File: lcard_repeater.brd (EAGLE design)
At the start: 100 x 80 mm, 90 parts, among them X1 236-741-5,08, X10 236-741-5,08, X11 236-741-5,08, X12 236-741-5,08, X13 236-741-5,08, X14 236-741-5,08, X15 236-741-5,08, X16 236-741-5,08, X17 236-741-5,08, X18 236-741-5,08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

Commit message: попытка развести плату
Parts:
- moved R1 11.6 mm to (39.4, 9.49)
- moved R10 11.6 mm to (35.6, 22.2)
- moved R11 11.6 mm to (31.8, 24.7)
- moved R13 11.6 mm to (39.4, 28.5)
- moved R14 11.6 mm to (35.6, 28.5)
- moved R15 11.6 mm to (31.8, 31.1)
- moved R17 11.6 mm to (39.4, 34.9)
- moved R18 11.6 mm to (35.6, 34.9)
- moved R19 11.6 mm to (31.8, 37.4)
- moved R2 11.6 mm to (35.6, 9.49)
- moved R21 11.6 mm to (39.4, 41.2)
- moved R22 11.6 mm to (35.6, 41.2)
- moved R23 11.6 mm to (31.8, 43.8)
- moved R25 11.6 mm to (39.4, 47.6), turned to 270 degrees
- moved R26 11.6 mm to (35.6, 47.6), turned to 270 degrees
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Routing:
- net GND: track 0.00 -> 98.8 mm, vias 0 -> 12
- net DAC1: track 0.00 -> 95.2 mm
- net DAC2: track 0.00 -> 58.2 mm
- net LY10: track 0.00 -> 50.3 mm, vias 0 -> 1
- net LY9: track 0.00 -> 47.1 mm, vias 0 -> 1
- net LY8: track 0.00 -> 43.2 mm, vias 0 -> 1
- net LY7: track 0.00 -> 40.0 mm, vias 0 -> 1
- net LX10: track 0.00 -> 35.9 mm
- net LY6: track 0.00 -> 35.6 mm, vias 0 -> 1
- net LX9: track 0.00 -> 32.2 mm
- net LY5: track 0.00 -> 30.6 mm, vias 0 -> 1
- net LY1: track 0.00 -> 30.3 mm, vias 0 -> 1
- net LY4: track 0.00 -> 29.1 mm, vias 0 -> 1
- net LX8: track 0.00 -> 28.7 mm
- net LY2: track 0.00 -> 26.8 mm, vias 0 -> 1
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
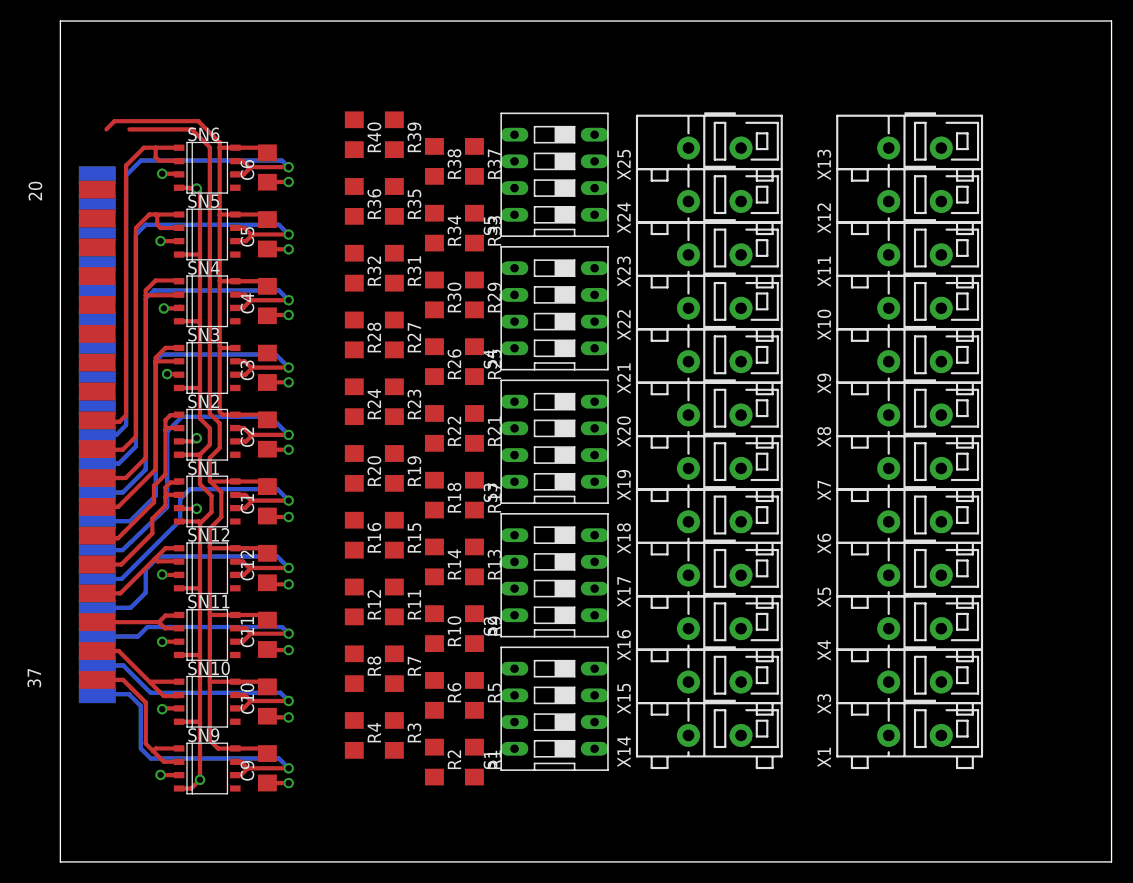
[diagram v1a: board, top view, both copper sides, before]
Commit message: почти развел плату, осталось немного. необходимо подсоединить конденсаторы по питанию
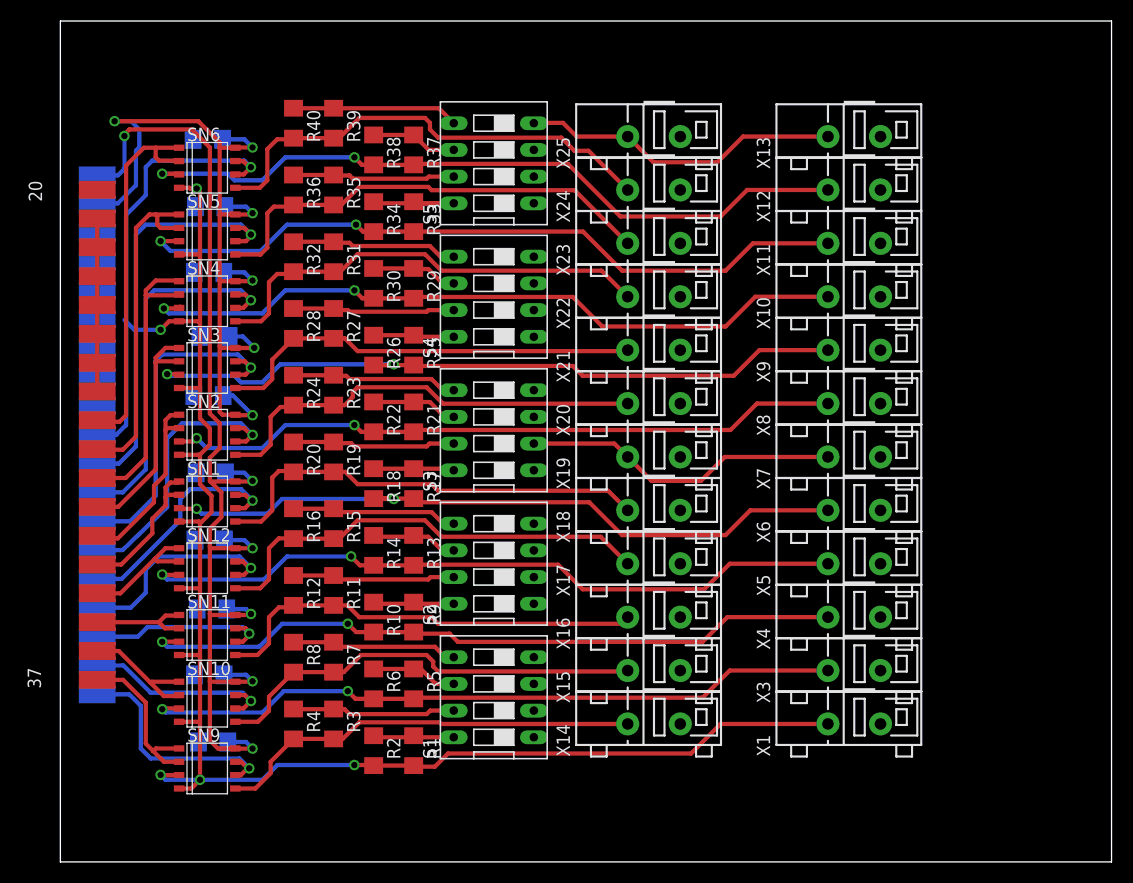
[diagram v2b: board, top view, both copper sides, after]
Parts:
- moved C2 6.71 mm to (14.1, 44.4), flipped to the bottom, turned to 180 degrees
- moved C6 6.27 mm to (14.0, 68.7), flipped to the bottom, turned to 180 degrees
- moved C4 6.19 mm to (14.1, 56.1), flipped to the bottom, turned to 180 degrees
- moved C12 6.09 mm to (14.2, 30.6), flipped to the bottom, turned to 180 degrees
- moved C10 6.09 mm to (14.2, 17.8), flipped to the bottom, turned to 180 degrees
- moved C5 6.05 mm to (14.2, 62.3), flipped to the bottom, turned to 180 degrees
- moved C1 6.03 mm to (14.3, 37.0), flipped to the bottom, turned to 180 degrees
- moved R10 5.88 mm to (29.8, 23.3)
- moved R14 5.88 mm to (29.8, 29.6)
- moved R18 5.88 mm to (29.8, 36.0)
- moved R2 5.88 mm to (29.8, 10.6)
- moved R22 5.88 mm to (29.8, 42.3)
- moved R26 5.88 mm to (29.8, 48.7)
- moved R30 5.88 mm to (29.8, 55.0)
- moved R34 5.88 mm to (29.8, 61.4)
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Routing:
- net GND: track 98.8 -> 178.1 mm, vias 12 -> 3
- net X7: track 1.16 -> 70.4 mm, vias 1 -> 2
- net X10: track 1.63 -> 69.6 mm, vias 1 -> 2
- net X9: track 1.77 -> 69.6 mm, vias 1 -> 2
- net X5: track 1.70 -> 69.0 mm, vias 1 -> 2
- net X8: track 1.78 -> 68.8 mm, vias 1 -> 2
- net X4: track 1.62 -> 68.4 mm, vias 1 -> 2
- net X3: track 1.61 -> 67.7 mm, vias 1 -> 2
- net X1: track 1.77 -> 67.8 mm, vias 1 -> 2
- net X2: track 1.64 -> 67.4 mm, vias 1 -> 2
- net X6: track 1.80 -> 64.5 mm, vias 1 -> 2
- net Y10: track 0.00 -> 45.0 mm
- net Y9: track 0.00 -> 44.1 mm
- net Y4: track 0.00 -> 43.5 mm
- net Y8: track 0.00 -> 43.4 mm
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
